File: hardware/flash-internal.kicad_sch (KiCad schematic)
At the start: 24 parts, among them U3 74LVC8T245, U4 74LVC8T245, U5 74LVC8T245, U6 S29AL016J55TFIR20, U7 74LVC8T245, U8 74LVC8T245

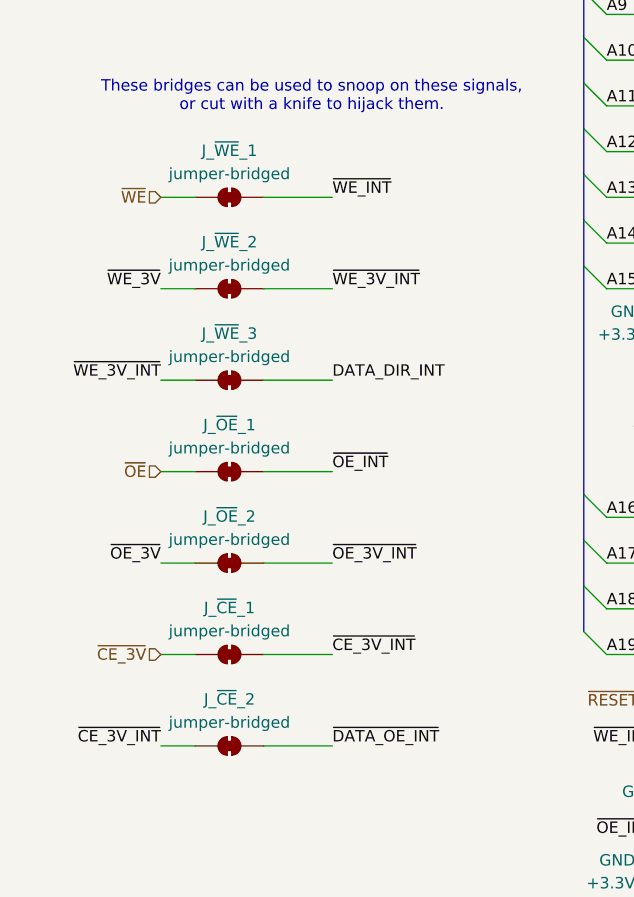
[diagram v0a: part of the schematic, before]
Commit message: Streamline cart board
 - Let JLCPCB populate the base header
 - Switch regulator for SMD version that JLCPCB can populate
 - Move components for easier routing, easier access to ammeter header
 - Add explanatory text in the silkscreen for each section of the PCB
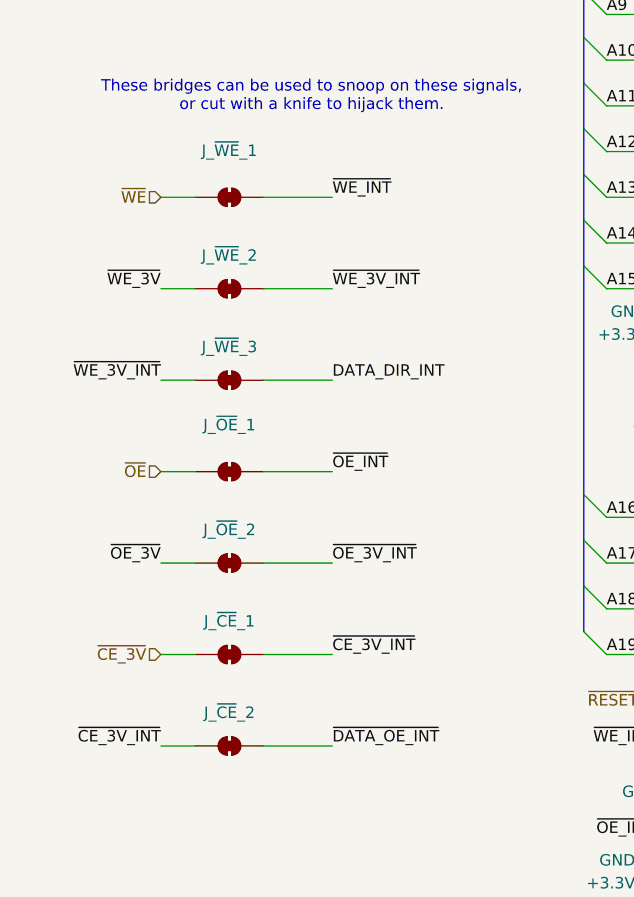
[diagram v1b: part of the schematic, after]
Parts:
- J_~{CE}_1, J_~{CE}_2, J_~{OE}_1, J_~{OE}_2, J_~{WE}_1, J_~{WE}_2, J_~{WE}_3: value jumper-bridged -> ~
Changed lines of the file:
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@@
 		(fields_autoplaced yes)
 		(property "Reference" "J_~{CE}_2"
-			(at 31.75 167.541 0)
+			(at 31.75 169.027 0)
 			(effects
 				(font
@@
 			)
 		)
-		(property "Value" "jumper-bridged"
-			(at 31.75 170.1108 0)
+		(property "Value" "~"
+			(at 31.75 170.8539 0)
 			(effects
 				(font
@@
 		(fields_autoplaced yes)
 		(property "Reference" "J_~{WE}_2"
-			(at 31.75 116.741 0)
+			(at 31.75 118.227 0)
 			(effects
 				(font
@@
 			)
 		)
-		(property "Value" "jumper-bridged"
-			(at 31.75 119.3108 0)
+		(property "Value" "~"
+			(at 31.75 120.0539 0)
 			(effects
 				(font
@@
 		(fields_autoplaced yes)
 		(property "Reference" "J_~{WE}_3"
-			(at 31.75 126.901 0)
+			(at 31.75 128.387 0)
 			(effects
 				(font
@@
 			)
 		)
-		(property "Value" "jumper-bridged"
-			(at 31.75 129.4708 0)
+		(property "Value" "~"
+			(at 31.75 130.2139 0)
 			(effects
 				(font
@@
 			)
 		)
-		(property "Value" "jumper-bridged"
+		(property "Value" "~"
 			(at 31.75 139.6308 0)
 			(effects
@@
 		(fields_autoplaced yes)
 		(property "Reference" "J_~{CE}_1"
-			(at 31.75 157.381 0)
+			(at 31.75 158.867 0)
 			(effects
 				(font
@@
 			)
 		)
-		(property "Value" "jumper-bridged"
-			(at 31.75 159.9508 0)
+		(property "Value" "~"
+			(at 31.75 160.6939 0)
 			(effects
 				(font
@@
 		(fields_autoplaced yes)
 		(property "Reference" "J_~{OE}_2"
-			(at 31.75 147.221 0)
+			(at 31.75 148.707 0)
 			(effects
 				(font
@@
 			)
 		)
-		(property "Value" "jumper-bridged"
-			(at 31.75 149.7908 0)
+		(property "Value" "~"
+			(at 31.75 150.5339 0)
 			(effects
 				(font
@@
 			)
 		)
-		(property "Value" "jumper-bridged"
+		(property "Value" "~"
 			(at 31.75 109.1508 0)
 			(effects

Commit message: Replace 8-bit buffers with cheaper version
Replace SN74LVC8T245DBR (8-bit buffers) with SN74LVC8T245PWR.  The old
version was SSOP, and the new version is a TSSOP size, but they are
otherwise the same.

This is estimated to reduce the price of a complete unit by over $11,
or about 16.5%.
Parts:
- U3, U4, U5, U7, U8: footprint Package_SO:SSOP-24_5.3x8.2mm_P0.65mm -> Package_SO:TSSOP-24_4.4x7.8mm_P0.65mm; JLCPCB Part Number C19197 -> C27643; Mouser Part Number 595-SN74LVC8T245DBR -> 595-SN74LVC8T245PWR; Part Number SN74LVC8T245DBR -> SN74LVC8T245PWR
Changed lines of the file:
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@@
 			)
 		)
-		(property "Footprint" "Package_SO:SSOP-24_5.3x8.2mm_P0.65mm"
+		(property "Footprint" "Package_SO:TSSOP-24_4.4x7.8mm_P0.65mm"
 			(at 238.76 129.54 0)
 			(effects
@@
 			)
 		)
-		(property "Datasheet" "https://www.ti.com/lit/ds/symlink/sn74lvc8t245.pdf"
+		(property "Datasheet" "https://www.ti.com/lit/gpn/sn74lvc8t245"
 			(at 218.44 140.97 0)
 			(effects
@@
 			)
 		)
-		(property "Mouser Part Number" "595-SN74LVC8T245DBR"
+		(property "Mouser Part Number" "595-SN74LVC8T245PWR"
 			(at 218.44 105.41 0)
 			(effects
@@
 			)
 		)
-		(property "Part Number" "SN74LVC8T245DBR"
+		(property "Part Number" "SN74LVC8T245PWR"
 			(at 218.44 105.41 0)
 			(effects
@@
 			)
 		)
-		(property "JLCPCB Part Number" "C19197"
+		(property "JLCPCB Part Number" "C27643"
 			(at 218.44 105.41 0)
 			(effects
@@
 			)
 		)
-		(property "Footprint" "Package_SO:SSOP-24_5.3x8.2mm_P0.65mm"
+		(property "Footprint" "Package_SO:TSSOP-24_4.4x7.8mm_P0.65mm"
 			(at 238.76 67.31 0)
 			(effects
@@
 			)
 		)
-		(property "Datasheet" "https://www.ti.com/lit/ds/symlink/sn74lvc8t245.pdf"
+		(property "Datasheet" "https://www.ti.com/lit/gpn/sn74lvc8t245"
 			(at 218.44 78.74 0)
 			(effects
@@
 			)
 		)
-		(property "Mouser Part Number" "595-SN74LVC8T245DBR"
+		(property "Mouser Part Number" "595-SN74LVC8T245PWR"
 			(at 218.44 43.18 0)
 			(effects
@@
 			)
 		)
-		(property "Part Number" "SN74LVC8T245DBR"
+		(property "Part Number" "SN74LVC8T245PWR"
 			(at 218.44 43.18 0)
 			(effects
@@
 			)
 		)
-		(property "JLCPCB Part Number" "C19197"
+		(property "JLCPCB Part Number" "C27643"
 			(at 218.44 43.18 0)
 			(effects
@@
 			)
 		)
-		(property "Footprint" "Package_SO:SSOP-24_5.3x8.2mm_P0.65mm"
+		(property "Footprint" "Package_SO:TSSOP-24_4.4x7.8mm_P0.65mm"
 			(at 113.03 128.27 0)
 			(effects
@@
 			)
 		)
-		(property "Datasheet" "https://www.ti.com/lit/ds/symlink/sn74lvc8t245.pdf"
+		(property "Datasheet" "https://www.ti.com/lit/gpn/sn74lvc8t245"
 			(at 92.71 139.7 0)
 			(effects
@@
 			)
 		)
-		(property "Mouser Part Number" "595-SN74LVC8T245DBR"
+		(property "Mouser Part Number" "595-SN74LVC8T245PWR"
 			(at 92.71 104.14 0)
 			(effects
@@
 			)
 		)
-		(property "Part Number" "SN74LVC8T245DBR"
+		(property "Part Number" "SN74LVC8T245PWR"
 			(at 92.71 104.14 0)
 			(effects
@@
 			)
 		)
-		(property "JLCPCB Part Number" "C19197"
+		(property "JLCPCB Part Number" "C27643"
 			(at 92.71 104.14 0)
 			(effects
@@
 			)
 		)
-		(property "Footprint" "Package_SO:SSOP-24_5.3x8.2mm_P0.65mm"
+		(property "Footprint" "Package_SO:TSSOP-24_4.4x7.8mm_P0.65mm"
 			(at 113.03 67.31 0)
 			(effects
@@
 			)
 		)
-		(property "Datasheet" "https://www.ti.com/lit/ds/symlink/sn74lvc8t245.pdf"
+		(property "Datasheet" "https://www.ti.com/lit/gpn/sn74lvc8t245"
 			(at 92.71 78.74 0)
 			(effects
@@
 			)
 		)
-		(property "Mouser Part Number" "595-SN74LVC8T245DBR"
+		(property "Mouser Part Number" "595-SN74LVC8T245PWR"
 			(at 92.71 43.18 0)
 			(effects
@@
 			)
 		)
-		(property "Part Number" "SN74LVC8T245DBR"
+		(property "Part Number" "SN74LVC8T245PWR"
 			(at 92.71 43.18 0)
 			(effects
@@
 			)
 		)
-		(property "JLCPCB Part Number" "C19197"
+		(property "JLCPCB Part Number" "C27643"
 			(at 92.71 43.18 0)
 			(effects
@@
 			)
 		)
-		(property "Footprint" "Package_SO:SSOP-24_5.3x8.2mm_P0.65mm"
+		(property "Footprint" "Package_SO:TSSOP-24_4.4x7.8mm_P0.65mm"
 			(at 113.03 189.23 0)
 			(effects
@@
 			)
 		)
-		(property "Datasheet" "https://www.ti.com/lit/ds/symlink/sn74lvc8t245.pdf"
+		(property "Datasheet" "https://www.ti.com/lit/gpn/sn74lvc8t245"
 			(at 92.71 200.66 0)
 			(effects
@@
 			)
 		)
-		(property "Mouser Part Number" "595-SN74LVC8T245DBR"
+		(property "Mouser Part Number" "595-SN74LVC8T245PWR"
 			(at 92.71 165.1 0)
 			(effects
@@
 			)
 		)
-		(property "Part Number" "SN74LVC8T245DBR"
+		(property "Part Number" "SN74LVC8T245PWR"
 			(at 92.71 165.1 0)
 			(effects
@@
 			)
 		)
-		(property "JLCPCB Part Number" "C19197"
+		(property "JLCPCB Part Number" "C27643"
 			(at 92.71 165.1 0)
 			(effects

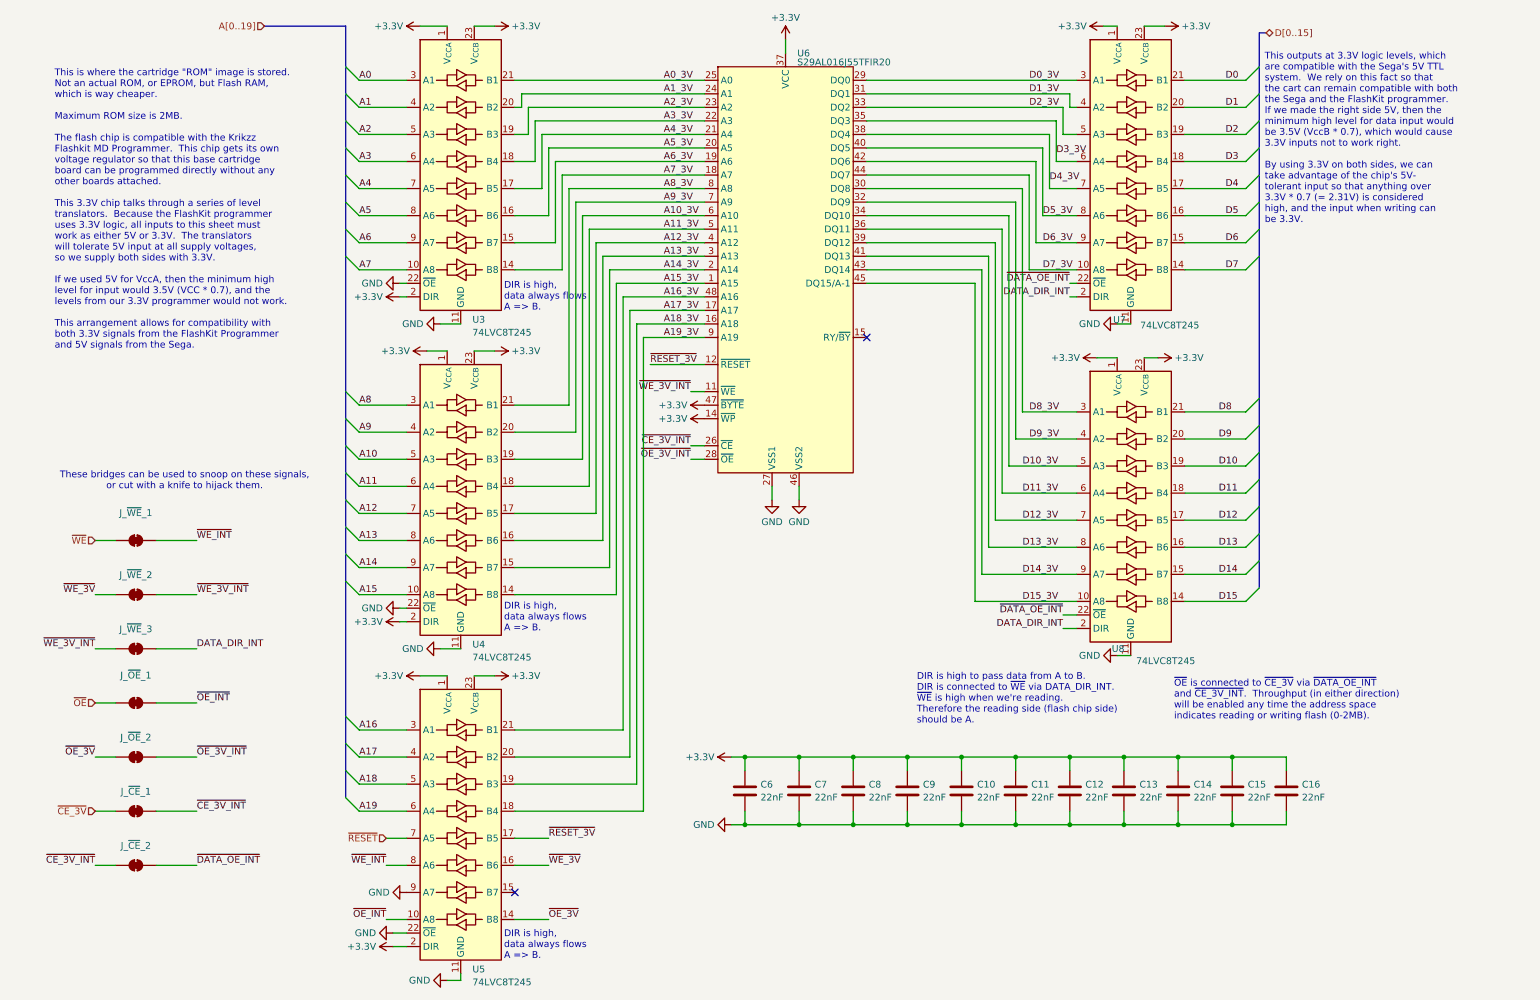
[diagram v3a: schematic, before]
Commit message: Move cart design into shareable subsheet
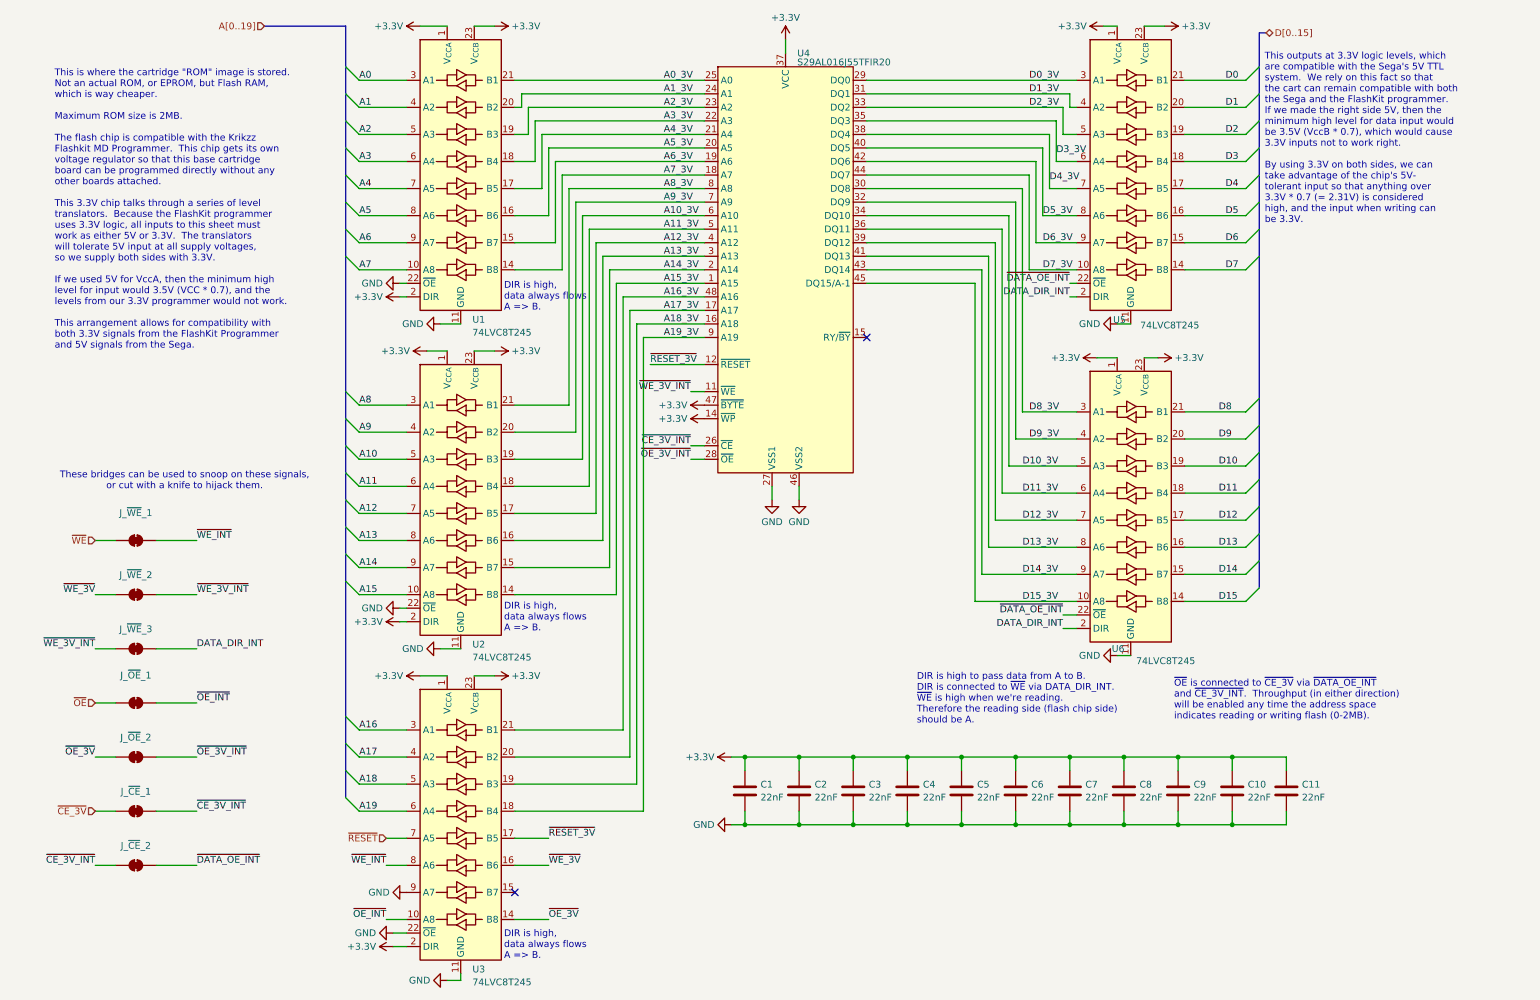
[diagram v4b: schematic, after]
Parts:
- renumbered C6 to C1, C15 to C10, C16 to C11, C7 to C2, C8 to C3, C9 to C4, C10 to C5, C11 to C6, C12 to C7, C13 to C8, C14 to C9, U3 to U1, U4 to U2, U5 to U3, U6 to U4, U7 to U5, U8 to U6

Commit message: Reannotate schematics and drop debug bridges
Parts are now numbered starting at 0 for cart, 100 for SRAM, 300 for
microcontroller.

Also, drop debug bridges that made routing more difficult and had the
same names across prototype boards.

Hopefully this will help avoid naming conflicts for the unified PCB.

Also, redo prototype PCB layouts.

Now that all the names have changed, update board layouts.
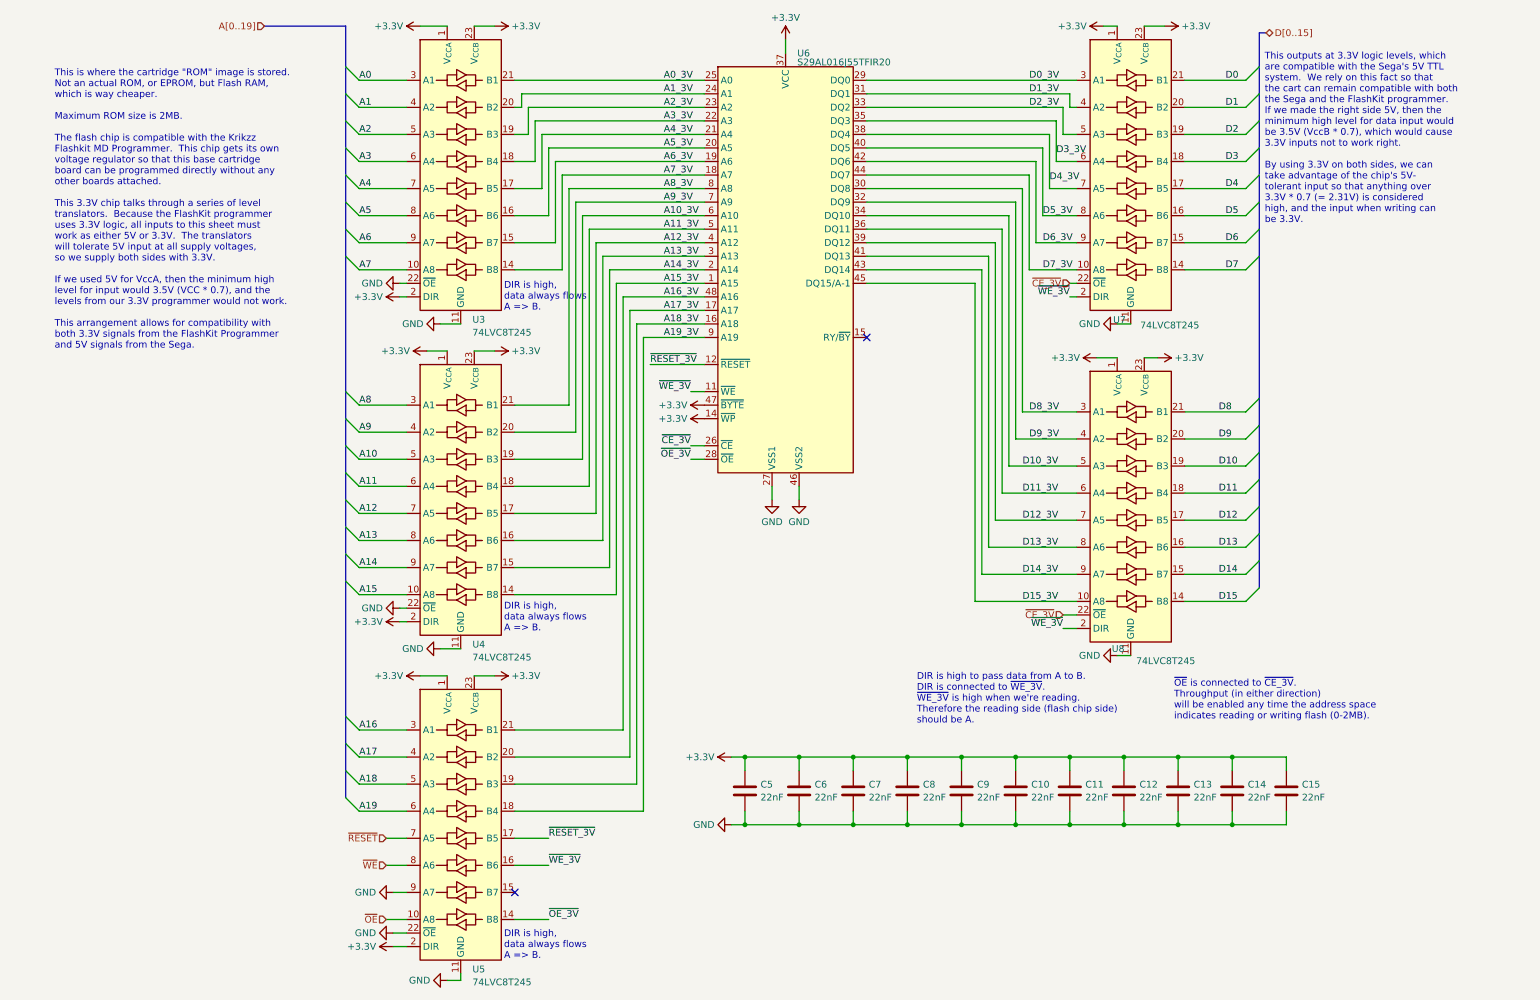
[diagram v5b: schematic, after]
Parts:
- removed J_~{CE}_1, J_~{CE}_2, J_~{OE}_1, J_~{OE}_2, J_~{WE}_1, J_~{WE}_2, J_~{WE}_3: ~, Jumper:SolderJumper-2_P1.3mm_Bridged_RoundedPad1.0x1.5mm, symbol Jumper:SolderJumper_2_Bridged
- renumbered C6 to C10, C7 to C11, C8 to C12, C9 to C13, C10 to C14, C11 to C15, C1 to C5, C2 to C6, C3 to C7, C4 to C8, C5 to C9, U1 to U3, U2 to U4, U3 to U5, U4 to U6, U5 to U7, U6 to U8
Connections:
- net DATA_DIR_INT is gone; now on net ~{WE_3V}: U7.2 (DIR), U8.2 (DIR)
- net ~{CE_3V_INT} is gone; now on net ~{CE_3V}: U6.26 (~{CE})
- net ~{DATA_OE_INT} is gone; now on net ~{CE_3V}: U7.22 (~{OE}), U8.22 (~{OE})
- net ~{OE_3V_INT} is gone; now on net ~{OE_3V}: U6.28 (~{OE})
- net ~{OE_INT} is gone; now on net ~{OE}: U5.10 (A8)
- net ~{WE_3V_INT} is gone; now on net ~{WE_3V}: U6.11 (~{WE})
- net ~{WE_INT} is gone; now on net ~{WE}: U5.8 (A6)
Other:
- note added: "DIR is high to pass data from A to B. DIR is connected to ~{WE_3V}. ~{WE_3V} is high when we're reading. Therefore the reading side (flash chip side) should be A."
- note added: "~{OE} is connected to ~{CE_3V}. Throughput (in either direction) will be enabled any time the address space indicates reading or writing flash (0-2MB)."
- note removed: "DIR is high to pass data from A to B. DIR is connected to ~{WE} via DATA_DIR_INT. ~{WE} is high when we're reading. Therefore the reading side (flash chip side) should be A."
- note removed: "These bridges can be used to snoop on these signals, or cut with a knife to hijack them."
- note removed: "~{OE} is connected to ~{CE_3V} via ~{DATA_OE_INT} and ~{CE_3V_INT}. Throughput (in either direction) will be enabled any time the address space indicates reading or writing flash (0-2MB)."
